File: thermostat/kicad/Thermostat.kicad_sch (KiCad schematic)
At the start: 8 parts

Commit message: Updating schematic and pinout doc.
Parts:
- C?: value (none) -> 2.2 uF
- R?: value (none) -> 570k
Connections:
- net +3V3: now also PIR?.3 (VCC)
- net at PIR?.2 (DATA): now also U?.7 (GPIO32)
- net at U?.15 (SD_CS): now also U?.15 (GPIO13); no longer U?.34 (GPIO3)
- net at U?.8 (LED): now also U?.29 (GPIO5); no longer U?.20 (GPIO6)
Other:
- moved on the sheet: PIR?

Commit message: Updated schematic to latest.
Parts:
- added C?: C_Polarized, symbol Device:C_Polarized
- R?: value 570k -> 4.7k
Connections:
- net +3V3: no longer PIR?.3 (VCC)
- net GNDREF: now also C?.2
- net at U?.19 (5V): now also C?.1
- new net +5V: PIR?.3 (VCC)
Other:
- note added: "Photoresistor"
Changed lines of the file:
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@@
+    (stroke (width 0) (type default) (color 0 0 0 0))
+  )
+  (wire (pts (xy 62.23 72.39) (xy 62.23 74.93))
     (stroke (width 0) (type default) (color 0 0 0 0))
   )
@@
     (stroke (width 0) (type default) (color 0 0 0 0))
   )
-  (wire (pts (xy 76.2 30.48) (xy 76.2 26.67))
+  (wire (pts (xy 76.2 22.86) (xy 76.2 30.48))
     (stroke (width 0) (type default) (color 0 0 0 0))
   )
@@
     (stroke (width 0) (type default) (color 0 0 0 0))
   )
+  (wire (pts (xy 62.23 82.55) (xy 62.23 85.09))
+    (stroke (width 0) (type default) (color 0 0 0 0))
+  )
   (wire (pts (xy 129.54 68.58) (xy 129.54 69.85))
     (stroke (width 0) (type default) (color 0 0 0 0))
@@
     (stroke (width 0) (type default) (color 0 0 0 0))
   )
+  (wire (pts (xy 71.12 72.39) (xy 62.23 72.39))
+    (stroke (width 0) (type default) (color 0 0 0 0))
+  )
   (wire (pts (xy 125.73 176.53) (xy 125.73 149.86))
     (stroke (width 0) (type default) (color 0 0 0 0))
@@
     (stroke (width 0) (type default) (color 0 0 0 0))
   )
-  (wire (pts (xy 129.54 77.47) (xy 129.54 81.28))
+  (wire (pts (xy 129.54 77.47) (xy 129.54 78.74))
     (stroke (width 0) (type default) (color 0 0 0 0))
   )
@@
     (stroke (width 0) (type default) (color 0 0 0 0))
   )
+  (wire (pts (xy 71.12 73.66) (xy 71.12 72.39))
+    (stroke (width 0) (type default) (color 0 0 0 0))
+  )
   (wire (pts (xy 143.51 46.99) (xy 143.51 52.07))
     (stroke (width 0) (type default) (color 0 0 0 0))
@@
   (wire (pts (xy 71.12 33.02) (xy 104.14 33.02))
     (stroke (width 0) (type default) (color 0 0 0 0))
+  )
+  (text "Photoresistor" (at 148.59 57.15 0)
+    (effects (font (size 1.27 1.27)) (justify left bottom))
   )
   (text "Thermostat" (at 181.61 170.18 0)
@@
     (pin "1")
     (pin "2")
+  )
+  (symbol (lib_id "power:GNDREF") (at 62.23 85.09 0) (unit 1)
+    (in_bom yes) (on_board yes) (fields_autoplaced)
+    (property "Reference" "#PWR?" (id 0) (at 62.23 91.44 0)
+      (effects (font (size 1.27 1.27)) hide)
+    )
+    (property "Value" "GNDREF" (id 1) (at 62.23 90.17 0)
+      (effects (font (size 1.27 1.27)) hide)
+    )
+    (property "Footprint" "" (id 2) (at 62.23 85.09 0)
+      (effects (font (size 1.27 1.27)) hide)
+    )
+    (property "Datasheet" "" (id 3) (at 62.23 85.09 0)
+      (effects (font (size 1.27 1.27)) hide)
+    )
+    (pin "1")
   )
   (symbol (lib_id "Pauls_Library:PIR_Motion_Sensor") (at 71.12 33.02 90) (unit 1)
@@
     (pin "1")
   )
-  (symbol (lib_id "power:+3V3") (at 76.2 26.67 0) (unit 1)
-    (in_bom yes) (on_board yes) (fields_autoplaced)
-    (property "Reference" "#PWR?" (id 0) (at 76.2 30.48 0)
-      (effects (font (size 1.27 1.27)) hide)
-    )
-    (property "Value" "+3V3" (id 1) (at 76.2 21.59 0))
-    (property "Footprint" "" (id 2) (at 76.2 26.67 0)
-      (effects (font (size 1.27 1.27)) hide)
-    )
-    (property "Datasheet" "" (id 3) (at 76.2 26.67 0)
+  (symbol (lib_id "power:+5V") (at 76.2 22.86 0) (unit 1)
+    (in_bom yes) (on_board yes) (fields_autoplaced)
+    (property "Reference" "#PWR?" (id 0) (at 76.2 26.67 0)
+      (effects (font (size 1.27 1.27)) hide)
+    )
+    (property "Value" "+5V" (id 1) (at 76.2 17.78 0))
+    (property "Footprint" "" (id 2) (at 76.2 22.86 0)
+      (effects (font (size 1.27 1.27)) hide)
+    )
+    (property "Datasheet" "" (id 3) (at 76.2 22.86 0)
       (effects (font (size 1.27 1.27)) hide)
     )
@@
       (effects (font (size 1.27 1.27)) (justify left))
     )
-    (property "Value" "570k" (id 1) (at 146.05 69.8499 0)
+    (property "Value" "4.7k" (id 1) (at 146.05 69.8499 0)
       (effects (font (size 1.27 1.27)) (justify left))
     )
@@
     )
     (property "Datasheet" "~" (id 3) (at 143.51 68.58 0)
+      (effects (font (size 1.27 1.27)) hide)
+    )
+    (pin "1")
+    (pin "2")
+  )
+  (symbol (lib_id "Device:C_Polarized") (at 62.23 78.74 0) (unit 1)
+    (in_bom yes) (on_board yes)
+    (property "Reference" "C?" (id 0) (at 64.77 76.2 0)
+      (effects (font (size 1.27 1.27)) (justify left))
+    )
+    (property "Value" "C_Polarized" (id 1) (at 66.04 79.1209 0)
+      (effects (font (size 1.27 1.27)) (justify left) hide)
+    )
+    (property "Footprint" "" (id 2) (at 63.1952 82.55 0)
+      (effects (font (size 1.27 1.27)) hide)
+    )
+    (property "Datasheet" "~" (id 3) (at 62.23 78.74 0)
       (effects (font (size 1.27 1.27)) hide)
     )
@@
     (pin "1")
   )
-  (symbol (lib_id "power:GNDREF") (at 129.54 81.28 0) (unit 1)
-    (in_bom yes) (on_board yes) (fields_autoplaced)
-    (property "Reference" "#PWR?" (id 0) (at 129.54 87.63 0)
-      (effects (font (size 1.27 1.27)) hide)
-    )
-    (property "Value" "GNDREF" (id 1) (at 129.54 86.36 0))
-    (property "Footprint" "" (id 2) (at 129.54 81.28 0)
-      (effects (font (size 1.27 1.27)) hide)
-    )
-    (property "Datasheet" "" (id 3) (at 129.54 81.28 0)
+  (symbol (lib_id "power:GNDREF") (at 129.54 78.74 0) (unit 1)
+    (in_bom yes) (on_board yes) (fields_autoplaced)
+    (property "Reference" "#PWR?" (id 0) (at 129.54 85.09 0)
+      (effects (font (size 1.27 1.27)) hide)
+    )
+    (property "Value" "GNDREF" (id 1) (at 129.54 83.82 0)
+      (effects (font (size 1.27 1.27)) hide)
+    )
+    (property "Footprint" "" (id 2) (at 129.54 78.74 0)
+      (effects (font (size 1.27 1.27)) hide)
+    )
+    (property "Datasheet" "" (id 3) (at 129.54 78.74 0)
       (effects (font (size 1.27 1.27)) hide)
     )
@@
   )
   (symbol_instances
+    (path "/2a7a8f97-978d-4463-89b9-3389a05b4193"
+      (reference "#PWR?") (unit 1) (value "GNDREF") (footprint "")
+    )
     (path "/3e437572-a035-4888-9fa9-b8423e265709"
       (reference "#PWR?") (unit 1) (value "GNDREF") (footprint "")
@@
       (reference "#PWR?") (unit 1) (value "GNDREF") (footprint "")
     )
-    (path "/69921c08-672a-4cab-9ef8-75bc920d0409"
-      (reference "#PWR?") (unit 1) (value "+3V3") (footprint "")
+    (path "/6b704bd5-43b0-4e87-9278-f36d38b3bfc2"
+      (reference "#PWR?") (unit 1) (value "+5V") (footprint "")
     )
     (path "/8cbd679a-e057-4633-9add-c60f4252f236"
@@
       (reference "C?") (unit 1) (value "2.2 uF") (footprint "")
     )
+    (path "/9e0c2c99-dad3-4a18-818b-54bc9e759a14"
+      (reference "C?") (unit 1) (value "C_Polarized") (footprint "")
+    )
     (path "/3ba1a0e3-fd82-4a75-baf4-b4be0e5073d7"
       (reference "PIR?") (unit 1) (value "PIR_Motion_Sensor") (footprint "")
     )
     (path "/9d8847e2-25c9-4bdd-b6ca-4df02570da76"
-      (reference "R?") (unit 1) (value "570k") (footprint "")
+      (reference "R?") (unit 1) (value "4.7k") (footprint "")
     )
     (path "/ae0a4f79-64f3-4f95-a69f-057259b61f40"

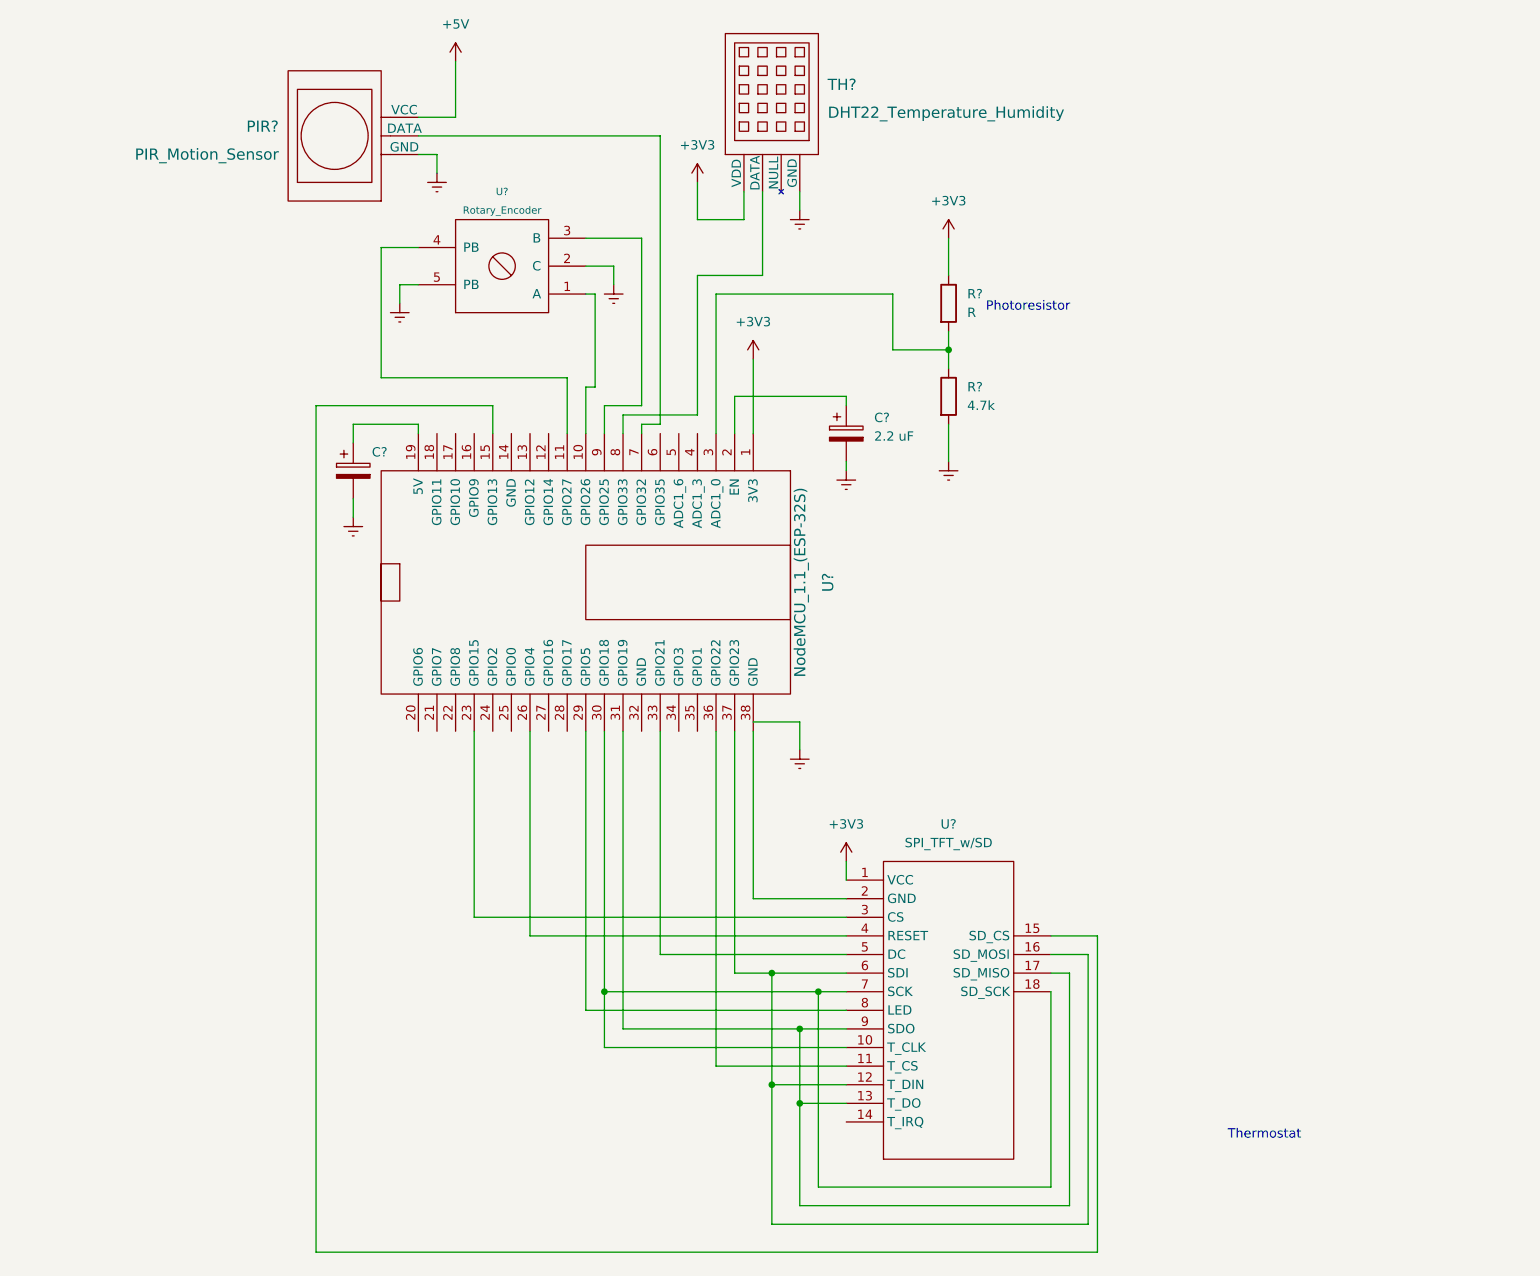
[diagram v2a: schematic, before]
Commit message: Thermostat: Minor documentation updates.
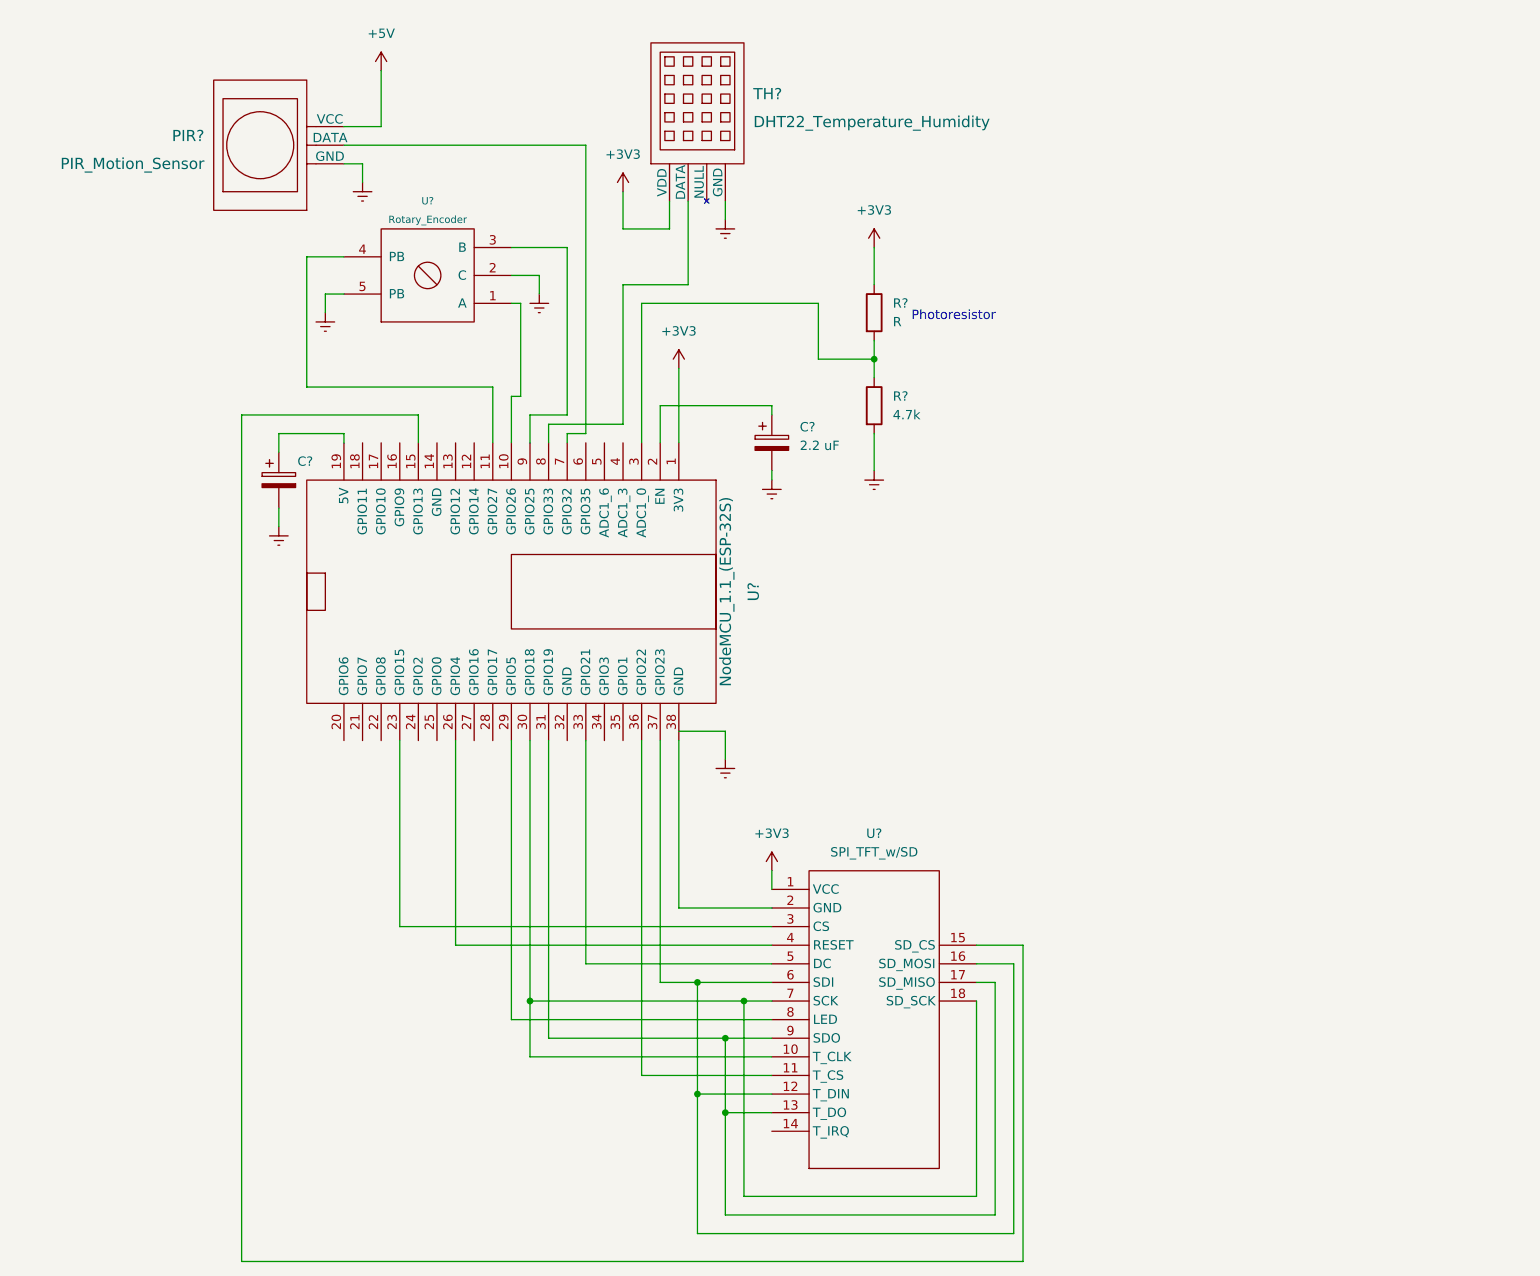
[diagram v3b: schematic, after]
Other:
- note removed: "Thermostat"
- title: (none) -> Thermostat
- moved on the sheet: C?, PIR?, R?, TH?, U?
